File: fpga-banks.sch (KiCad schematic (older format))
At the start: 14 parts, among them U1 XC7K70T-FBG484, U2 ASEM1-100.000MHZ-LC-T

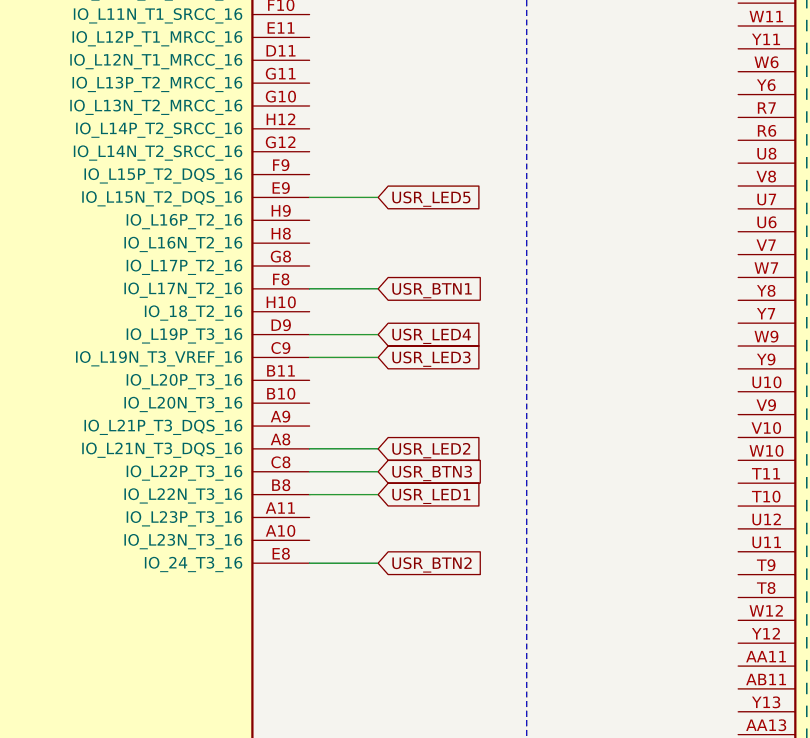
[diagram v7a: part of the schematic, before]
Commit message: Update buttons and LEDs connection
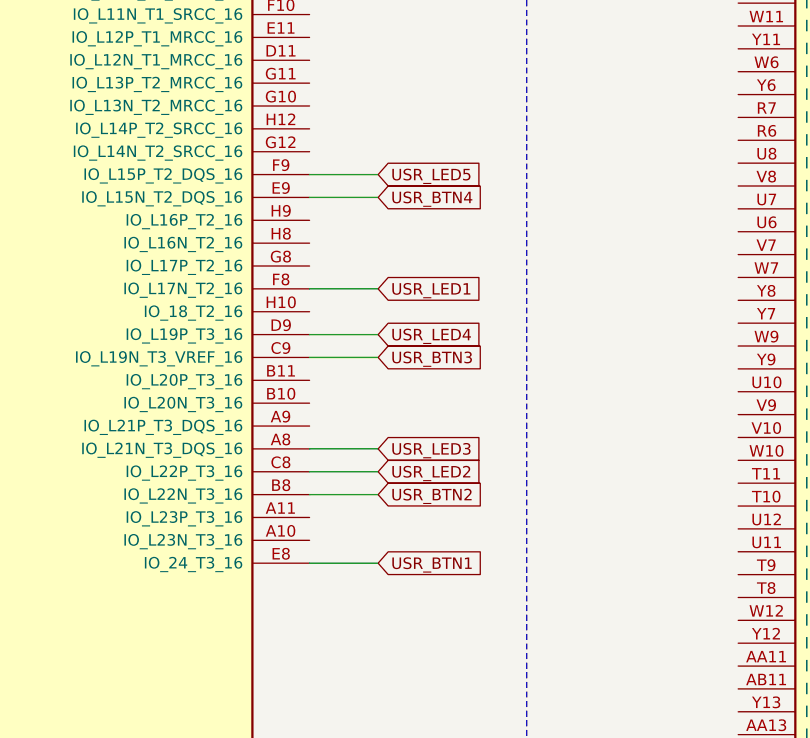
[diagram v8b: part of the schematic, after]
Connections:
- net USR_BTN1: now also U1.E8 (IO_24_T3_16); no longer U1.F8 (IO_L17N_T2_16)
- net USR_BTN2: now also U1.B8 (IO_L22N_T3_16); no longer U1.E8 (IO_24_T3_16)
- net USR_BTN3: now also U1.C9 (IO_L19N_T3_VREF_16); no longer U1.C8 (IO_L22P_T3_16)
- net USR_LED1: now also U1.F8 (IO_L17N_T2_16); no longer U1.B8 (IO_L22N_T3_16)
- net USR_LED2: now also U1.C8 (IO_L22P_T3_16); no longer U1.A8 (IO_L21N_T3_DQS_16)
- net USR_LED3: now also U1.A8 (IO_L21N_T3_DQS_16); no longer U1.C9 (IO_L19N_T3_VREF_16)
- net USR_LED5: now also U1.F9 (IO_L15P_T2_DQS_16); no longer U1.E9 (IO_L15N_T2_DQS_16)
- new net USR_BTN4: U1.E9 (IO_L15N_T2_DQS_16)
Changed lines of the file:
@@
 Text Notes 5950 2950 1    50   ~ 0
 config-spi.sch
-Text GLabel 10525 5375 2    50   Input ~ 0
+Text GLabel 10525 4475 2    50   Input ~ 0
 USR_LED1
+Text GLabel 10525 5275 2    50   Input ~ 0
+USR_LED2
 Text GLabel 10525 5175 2    50   Input ~ 0
-USR_LED2
-Text GLabel 10525 4775 2    50   Input ~ 0
 USR_LED3
-Text GLabel 10525 4075 2    50   Input ~ 0
+Text GLabel 10525 3975 2    50   Input ~ 0
 USR_LED5
 Wire Wire Line
@@
 CSI_B used for config
 Wire Wire Line
-	10525 5375 10225 5375
+	10525 4475 10225 4475
+Wire Wire Line
+	10225 5275 10525 5275
+Wire Wire Line
+	10225 3975 10525 3975
 Wire Wire Line
 	10225 5175 10525 5175
-Wire Wire Line
-	10225 4075 10525 4075
-Wire Wire Line
-	10225 4775 10525 4775
 Wire Wire Line
 	4800 3400 5300 3400
@@
 Text GLabel 15500 6925 2    50   Input ~ 0
 CA2_A
-Text GLabel 10525 4475 2    50   Input ~ 0
+Text GLabel 10525 5675 2    50   Input ~ 0
 USR_BTN1
-Text GLabel 10525 5675 2    50   Input ~ 0
+Text GLabel 10525 5375 2    50   Input ~ 0
 USR_BTN2
-Text GLabel 10525 5275 2    50   Input ~ 0
+Text GLabel 10525 4775 2    50   Input ~ 0
 USR_BTN3
 Wire Wire Line
-	10225 4475 10525 4475
-Wire Wire Line
 	10225 5675 10525 5675
 Wire Wire Line
-	10225 5275 10525 5275
+	10225 5375 10525 5375
+Wire Wire Line
+	10225 4775 10525 4775
 Wire Wire Line
 	10225 4675 10525 4675
@@
 NoConn ~ 15000 6025
 NoConn ~ 15000 7125
+Wire Wire Line
+	10225 4075 10525 4075
+Text GLabel 10525 4075 2    50   Input ~ 0
+USR_BTN4
 $EndSCHEMATC
